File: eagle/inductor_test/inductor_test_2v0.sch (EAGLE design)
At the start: 81 parts, among them J1 MA02-1, U1 OPA2369, U2 OPA2369, U3 SC70, U4 SOT-23-6, U5 TSSOP-14, U6 TPS62122, U7 MAX9910

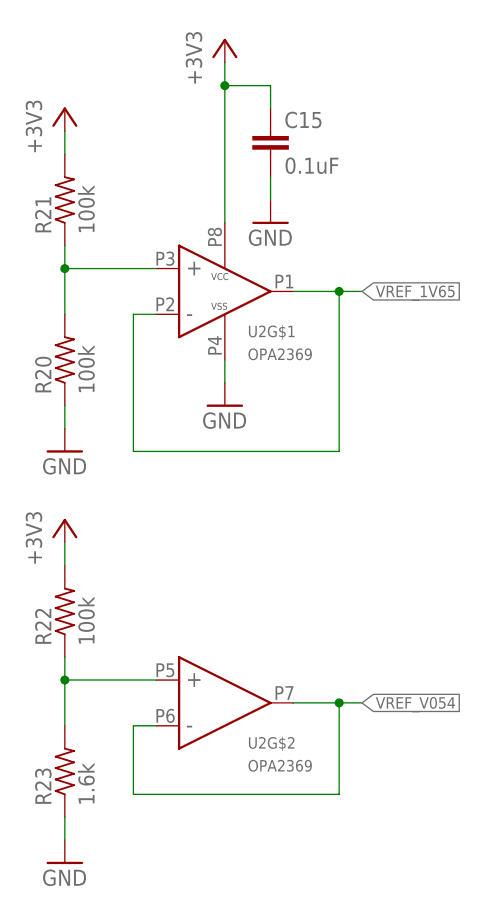
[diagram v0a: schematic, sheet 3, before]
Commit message: finished adding part numbers for inductor test board
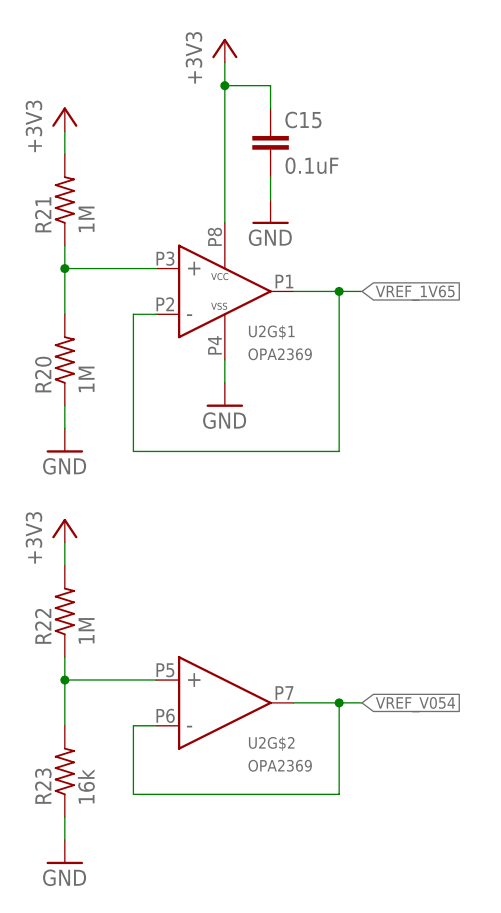
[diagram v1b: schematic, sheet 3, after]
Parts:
- C1, C6, C7, C8: DIGIKEY (none) -> 445-13815-1-ND
- C10, C11, C12, C13, C2, C9: DIGIKEY (none) -> 1276-1450-1-ND
- C14, C15, C22, C3, C4, C5: DIGIKEY (none) -> 445-4952-1-ND
- L1, L2, L3, L4, L5: DIGIKEY (none) -> 732-3452-1-ND
- R1, R12, R13, R5: DIGIKEY (none) -> P20.0KLCT-ND
- R10, R6, R9: DIGIKEY (none) -> P4.99KLCT-ND; DIGIKEY_2 (none) -> 541-1.30MLCT-ND
- R11, R7, R8: DIGIKEY (none) -> RMCF0402FT4R99CT-ND; DIGIKEY_2 (none) -> P1.00KLCT-ND
- R14, R16, R18: DIGIKEY (none) -> P887KLCT-ND
- R15, R17, R19: DIGIKEY (none) -> P30.0KLCT-ND
- R2: DIGIKEY (none) -> P200LCT-ND
- R20, R21, R22: value 100k -> 1M; DIGIKEY (none) -> P1.00MLCT-ND
- R23: value 1.6k -> 16k; DIGIKEY (none) -> P16.0KLCT-ND
- R27, R28: DIGIKEY (none) -> P10KGCT-ND
- R29, R30: DIGIKEY (none) -> P10GCT-ND
- R3: DIGIKEY (none) -> P1.00MLCT-ND
- R31: DIGIKEY (none) -> P240GCT-ND
- R4: DIGIKEY (none) -> P75.0LCT-ND
- TP16: DIGIKEY (none) -> 36-5013-ND
